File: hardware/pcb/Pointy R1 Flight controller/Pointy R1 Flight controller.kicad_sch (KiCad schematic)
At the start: 30 parts, among them IC1 TEENSY_4.1, J3 XT60-M, M1 Motor_Servo, M2 Motor_Servo, P1 282837-2, P2 282837-2, P3 282837-2, P5 282837-2, Q1 IRLZ44NSTRLPBF, Q2 IRLZ44NSTRLPBF, Q3 IRLZ44NSTRLPBF, U1 L7805CV, U2 GY-521, U3 MPL3115A2

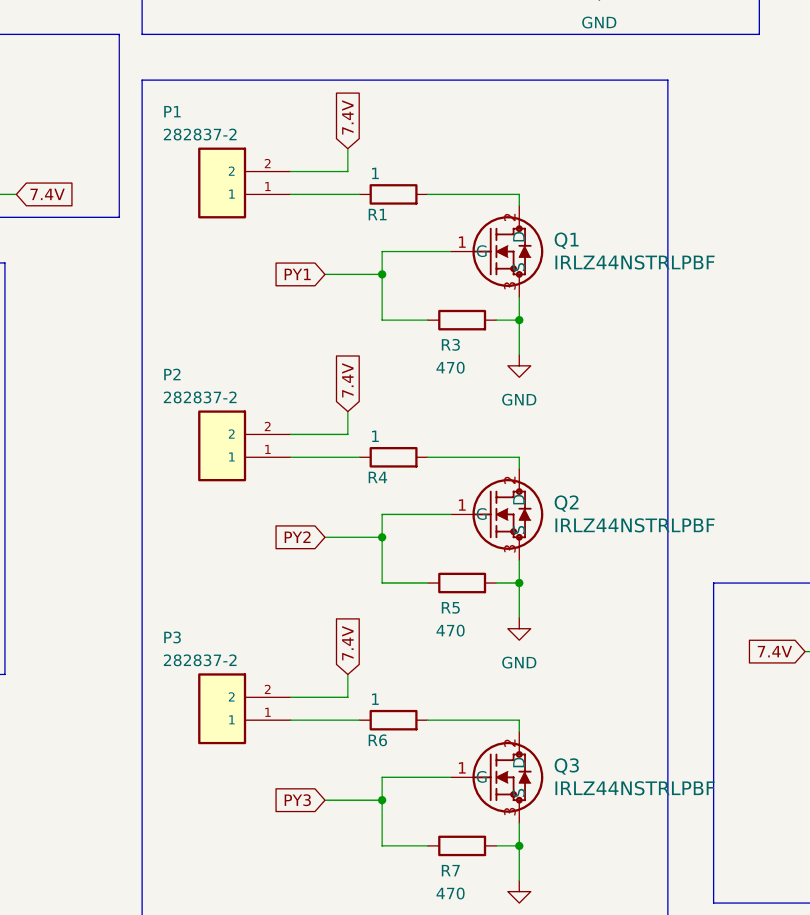
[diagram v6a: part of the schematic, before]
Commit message: Added 1N4007 flyback diodes for over voltage/current protection on mosfets
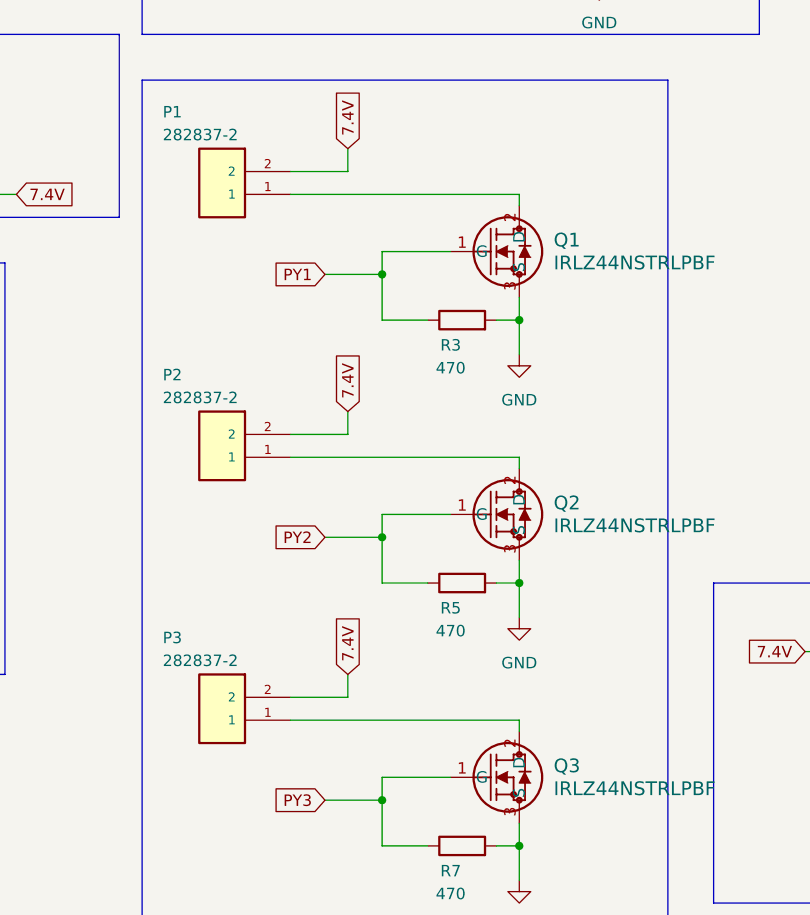
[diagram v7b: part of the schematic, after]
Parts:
- removed R1, R4, R6: 1, Resistor_SMD:R_0805_2012Metric, symbol Device:R
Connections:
- net at P2.1: now also Q2.2 (D)
- net at Q1.2 (D): now also P1.1
- net at P3.1: now also Q3.2 (D)
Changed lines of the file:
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@@
 	(wire
 		(pts
-			(xy 100.33 124.46) (xy 110.49 124.46)
-		)
-		(stroke
-			(width 0)
-			(type default)
-		)
-	)
-	(wire
-		(pts
 			(xy 30.48 99.06) (xy 35.56 99.06)
 		)
@@
 	(wire
 		(pts
-			(xy 100.33 66.04) (xy 110.49 66.04)
-		)
-		(stroke
-			(width 0)
-			(type default)
-		)
-	)
-	(wire
-		(pts
 			(xy 36.83 30.48) (xy 45.72 30.48)
 		)
@@
 	(wire
 		(pts
-			(xy 85.09 95.25) (xy 92.71 95.25)
+			(xy 85.09 95.25) (xy 110.49 95.25)
 		)
 		(stroke
@@
 	(wire
 		(pts
-			(xy 85.09 66.04) (xy 92.71 66.04)
+			(xy 85.09 66.04) (xy 110.49 66.04)
 		)
 		(stroke
@@
 	(wire
 		(pts
-			(xy 85.09 124.46) (xy 92.71 124.46)
+			(xy 85.09 124.46) (xy 110.49 124.46)
 		)
 		(stroke
@@
 	(wire
 		(pts
-			(xy 100.33 95.25) (xy 110.49 95.25)
-		)
-		(stroke
-			(width 0)
-			(type default)
-		)
-	)
-	(wire
-		(pts
 			(xy 95.25 101.6) (xy 95.25 104.14)
 		)
@@
 	)
 	(symbol
-		(lib_id "Device:R")
-		(at 96.52 95.25 90)
-		(unit 1)
-		(exclude_from_sim no)
-		(in_bom yes)
-		(on_board yes)
-		(dnp no)
-		(property "Reference" "R4"
-			(at 94.742 97.536 90)
-			(effects
-				(font
-					(size 1.27 1.27)
-				)
-			)
-		)
-		(property "Value" "1"
-			(at 94.488 92.964 90)
-			(effects
-				(font
-					(size 1.27 1.27)
-				)
-			)
-		)
-		(property "Footprint" "Resistor_SMD:R_0805_2012Metric"
-			(at 96.52 97.028 90)
-			(effects
-				(font
-					(size 1.27 1.27)
-				)
-				(hide yes)
-			)
-		)
-		(property "Datasheet" "~"
-			(at 96.52 95.25 0)
-			(effects
-				(font
-					(size 1.27 1.27)
-				)
-				(hide yes)
-			)
-		)
-		(property "Description" "Resistor"
-			(at 96.52 95.25 0)
-			(effects
-				(font
-					(size 1.27 1.27)
-				)
-				(hide yes)
-			)
-		)
-		(pin "2"
-		)
-		(pin "1"
-		)
-		(instances
-			(project "Pointy R1 Flight controller"
-				(path "/461b38ed-136a-4336-8029-84a41326c46a"
-					(reference "R4")
-					(unit 1)
-				)
-			)
-		)
-	)
-	(symbol
 		(lib_id "power:+5V")
 		(at 132.08 22.86 0)
@@
 	)
 	(symbol
-		(lib_id "Device:R")
-		(at 96.52 66.04 90)
-		(unit 1)
-		(exclude_from_sim no)
-		(in_bom yes)
-		(on_board yes)
-		(dnp no)
-		(property "Reference" "R1"
-			(at 94.742 68.326 90)
-			(effects
-				(font
-					(size 1.27 1.27)
-				)
-			)
-		)
-		(property "Value" "1"
-			(at 94.488 63.754 90)
-			(effects
-				(font
-					(size 1.27 1.27)
-				)
-			)
-		)
-		(property "Footprint" "Resistor_SMD:R_0805_2012Metric"
-			(at 96.52 67.818 90)
-			(effects
-				(font
-					(size 1.27 1.27)
-				)
-				(hide yes)
-			)
-		)
-		(property "Datasheet" "~"
-			(at 96.52 66.04 0)
-			(effects
-				(font
-					(size 1.27 1.27)
-				)
-				(hide yes)
-			)
-		)
-		(property "Description" "Resistor"
-			(at 96.52 66.04 0)
-			(effects
-				(font
-					(size 1.27 1.27)
-				)
-				(hide yes)
-			)
-		)
-		(pin "2"
-		)
-		(pin "1"
-		)
-		(instances
-			(project ""
-				(path "/461b38ed-136a-4336-8029-84a41326c46a"
-					(reference "R1")
-					(unit 1)
-				)
-			)
-		)
-	)
-	(symbol
 		(lib_id "power:+5V")
 		(at 193.04 144.78 0)
@@
 					(unit 1)
 				)
-			)
-		)
-	)
-	(symbol
-		(lib_id "Device:R")
-		(at 96.52 124.46 90)
-		(unit 1)
-		(exclude_from_sim no)
-		(in_bom yes)
-		(on_board yes)
-		(dnp no)
-		(property "Reference" "R6"
-			(at 94.742 126.746 90)
-			(effects
-				(font
-					(size 1.27 1.27)
-				)
-			)
-		)
-		(property "Value" "1"
-			(at 94.488 122.174 90)
-			(effects
-				(font
-					(size 1.27 1.27)
-				)
-			)
-		)
-		(property "Footprint" "Resistor_SMD:R_0805_2012Metric"
-			(at 96.52 126.238 90)
-			(effects
-				(font
-					(size 1.27 1.27)
-				)
-				(hide yes)
-			)
-		)
-		(property "Datasheet" "~"
-			(at 96.52 124.46 0)
-			(effects
-				(font
-					(size 1.27 1.27)
-				)
-				(hide yes)
-			)
-		)
-		(property "Description" "Resistor"
-			(at 96.52 124.46 0)
-			(effects
-				(font
-					(size 1.27 1.27)
-				)
-				(hide yes)
-			)
-		)
-		(pin "2"
-		)
-		(pin "1"
-		)
-		(instances
-			(project "Pointy R1 Flight controller"
-				(path "/461b38ed-136a-4336-8029-84a41326c46a"
-					(reference "R6")
-					(unit 1)
-				)

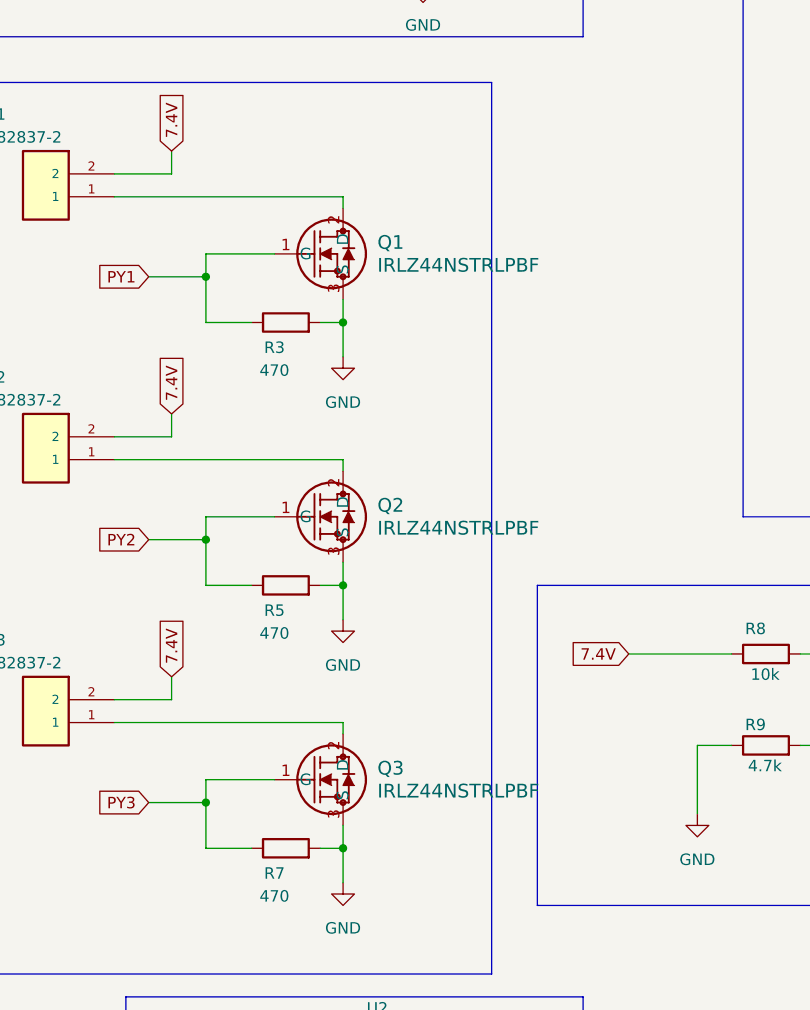
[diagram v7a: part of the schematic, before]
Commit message: Added 1N4007 flyback diodes to schematic + made neccisary connections
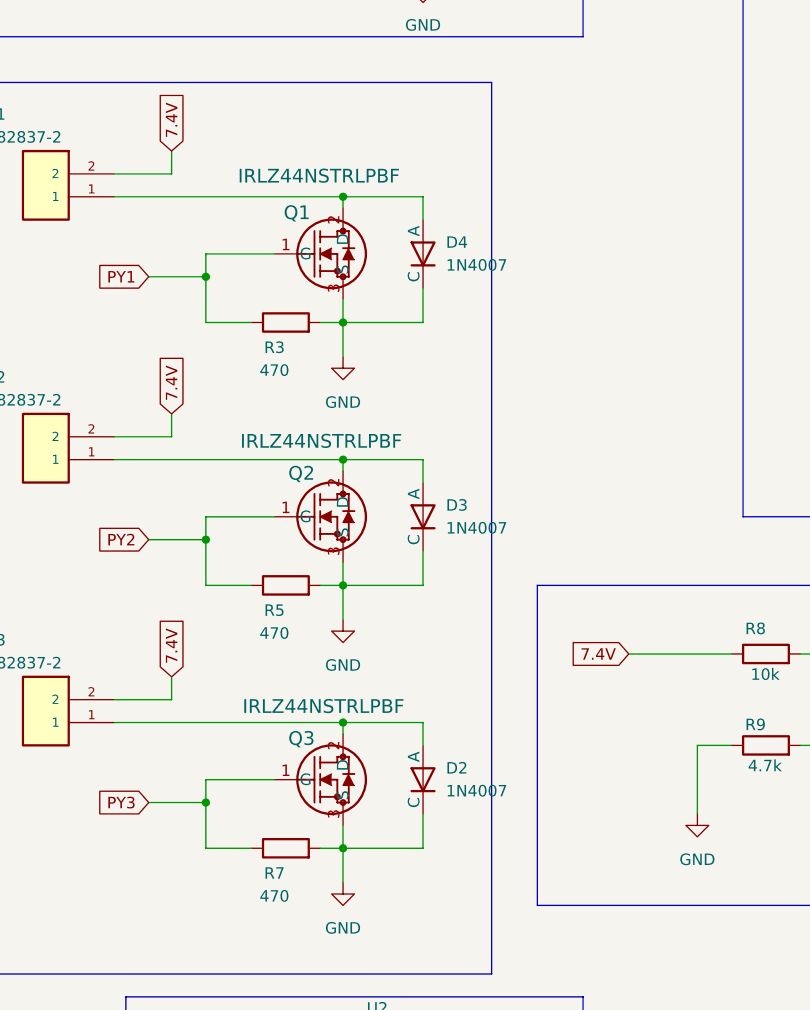
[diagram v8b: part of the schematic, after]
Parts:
- added D2, D3, D4: 1N4007, footprints:P1_DO-41, symbol symbols:1N4007 Diode
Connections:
- net GND: now also D2.2 (C), D3.2 (C), D4.2 (C)
- net at P2.1, Q2.2 (D): now also D3.1 (A)
- net at P1.1, Q1.2 (D): now also D4.1 (A)
- net at P3.1, Q3.2 (D): now also D2.1 (A)
